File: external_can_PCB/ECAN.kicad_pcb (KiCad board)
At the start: 4 copper layers, 39.6 x 49.5 mm, 38 parts, among them J1 JST GH 4, J3 JST GH 6, J4 Micro_SD_Card, J5 JST GH 6, U1 SN65HVD232, U2 AP2127N-3.3, U5 STM32L562RETx, Y1 8 Mhz

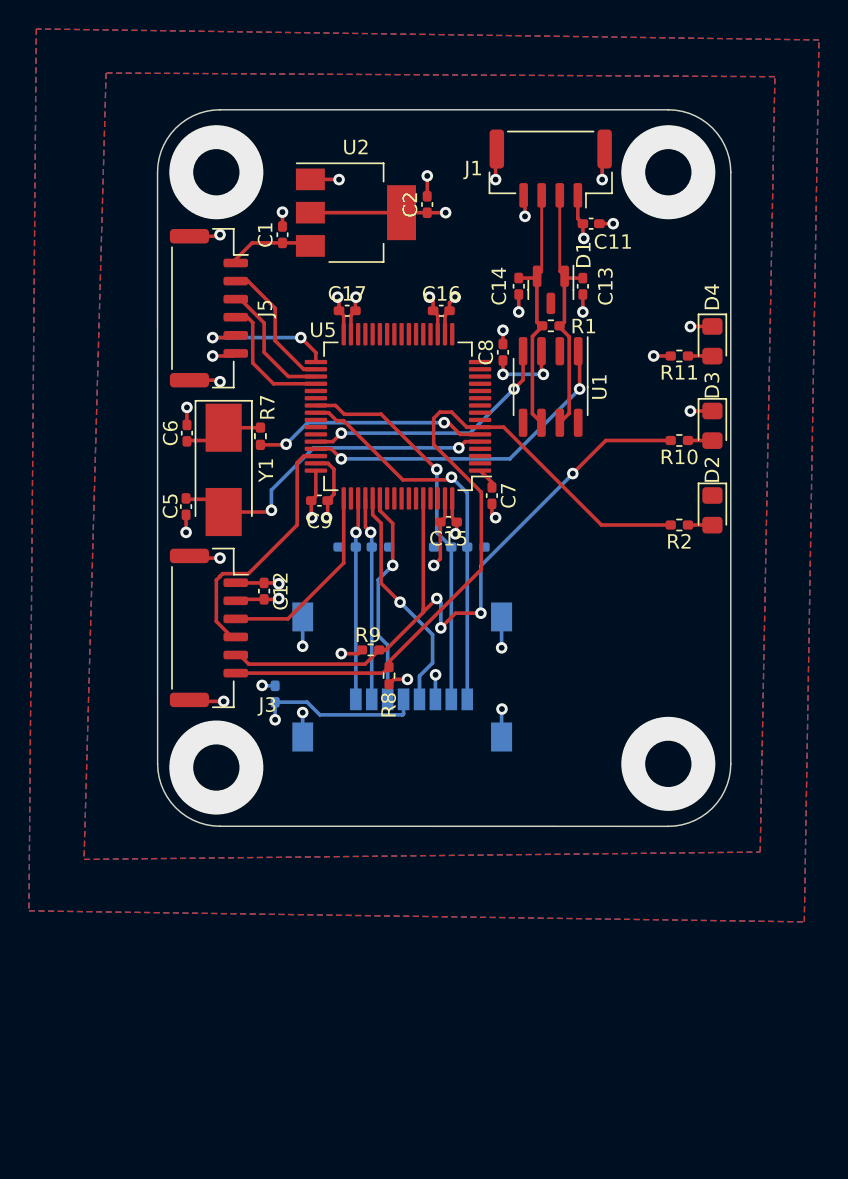
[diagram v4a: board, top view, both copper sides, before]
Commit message: Addressed issues from Review by Olof
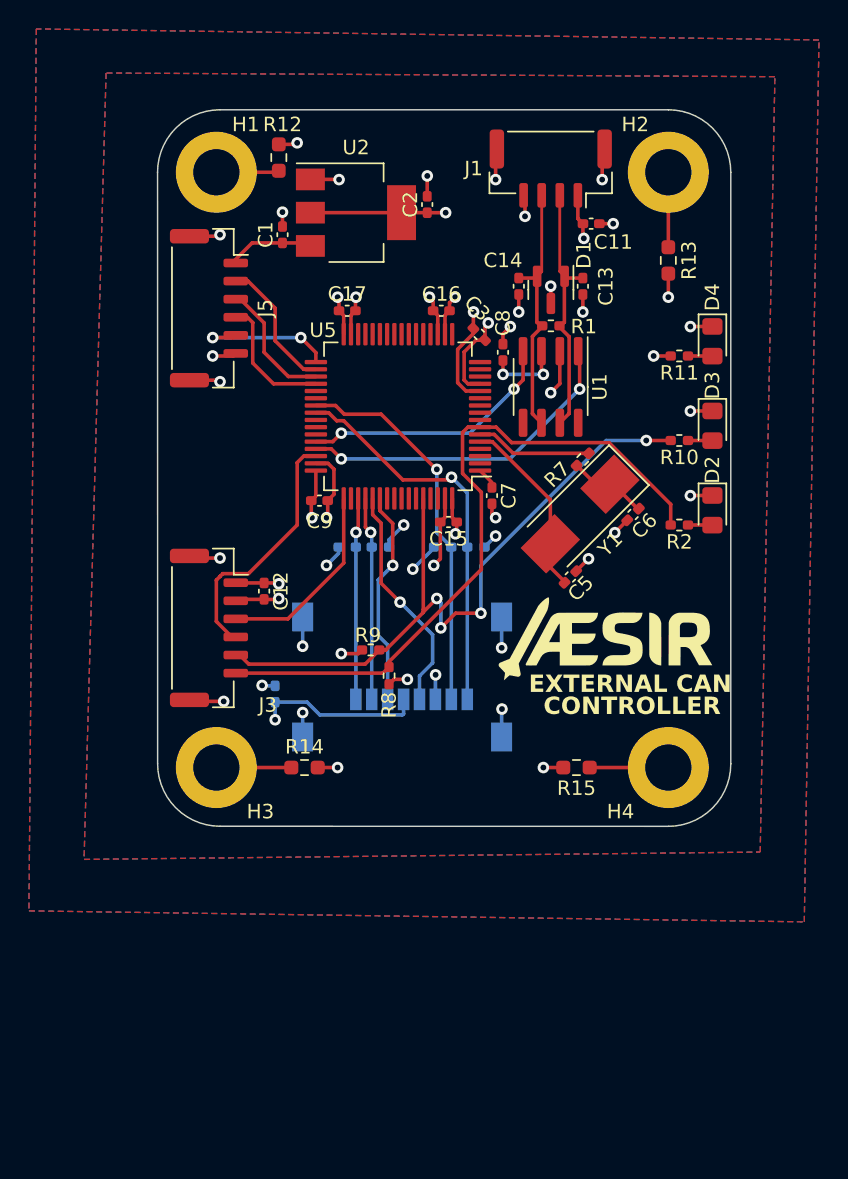
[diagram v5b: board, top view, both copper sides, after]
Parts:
- added C3: 0.1 uF, Capacitor_SMD:C_0402_1005Metric_Pad0.74x0.62mm_HandSolder, F.Cu at (142.6, 50.3)
- added G***: LOGO, LOGO, F.Cu at (151.4, 71.4)
- added H1: MountingHole_Pad, MountingHole:MountingHole_3.2mm_M3_DIN965_Pad, F.Cu at (124.5, 39.1)
- added H2: MountingHole_Pad, MountingHole:MountingHole_3.2mm_M3_DIN965_Pad, F.Cu at (155.7, 39.1)
- added H3: MountingHole_Pad, MountingHole:MountingHole_3.2mm_M3_DIN965_Pad, F.Cu at (124.5, 80.3)
- added H4: MountingHole_Pad, MountingHole:MountingHole_3.2mm_M3_DIN965_Pad, F.Cu at (155.7, 80.3)
- added R12: 1M, Resistor_SMD:R_0603_1608Metric_Pad0.98x0.95mm_HandSolder, F.Cu at (128.8, 38.1)
- added R13: 1M, Resistor_SMD:R_0603_1608Metric_Pad0.98x0.95mm_HandSolder, F.Cu at (155.7, 45.2)
- added R14: 1M, Resistor_SMD:R_0603_1608Metric_Pad0.98x0.95mm_HandSolder, F.Cu at (130.6, 80.3)
- added R15: 1M, Resistor_SMD:R_0603_1608Metric_Pad0.98x0.95mm_HandSolder, F.Cu at (149.4, 80.3)
- moved C6 31.3 mm to (153.3, 62.8), turned to -135 degrees
- moved C5 27.0 mm to (148.9, 67.1), turned to 45 degrees
- moved Y1 24.8 mm to (149.6, 62.7), turned to -135 degrees
- moved R7 22.3 mm to (149.8, 59.0), turned to -135 degrees
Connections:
- net /SPI3_MISO_3.3V renamed /SPI2_MISO_3.3V
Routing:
- net GND: track 60.9 -> 80.1 mm, vias 31 -> 39
- net +3.3V: track 47.6 -> 60.6 mm, vias 13 -> 18
- net Net-(U5-PH0): track 23.3 -> 12.3 mm, vias 2 -> 0
- net Net-(U5-PH1): track 16.2 -> 8.06 mm, vias 2 -> 0
- net Net-(H4-Pad1): track 0.00 -> 5.44 mm
- net Net-(H2-Pad1): track 0.00 -> 5.18 mm
- net Net-(H3-Pad1): track 0.00 -> 5.18 mm
- net Net-(H1-Pad1): track 0.00 -> 4.36 mm
- net /NRST: track 51.6 -> 48.2 mm
- net (no net): vias 4 -> 0
- added copper zone on B.Cu, net (none)
- added copper zone on F.Cu, net (none)
- removed copper zone on B.Cu, net /FDCAN1_RX
- removed copper zone on F.Cu, net /FDCAN1_RX
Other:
- board text added: "CONTROLLER"
- board text added: "EXTERNAL CAN"

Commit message: GPIO LED changes and UART connection to SPI lines
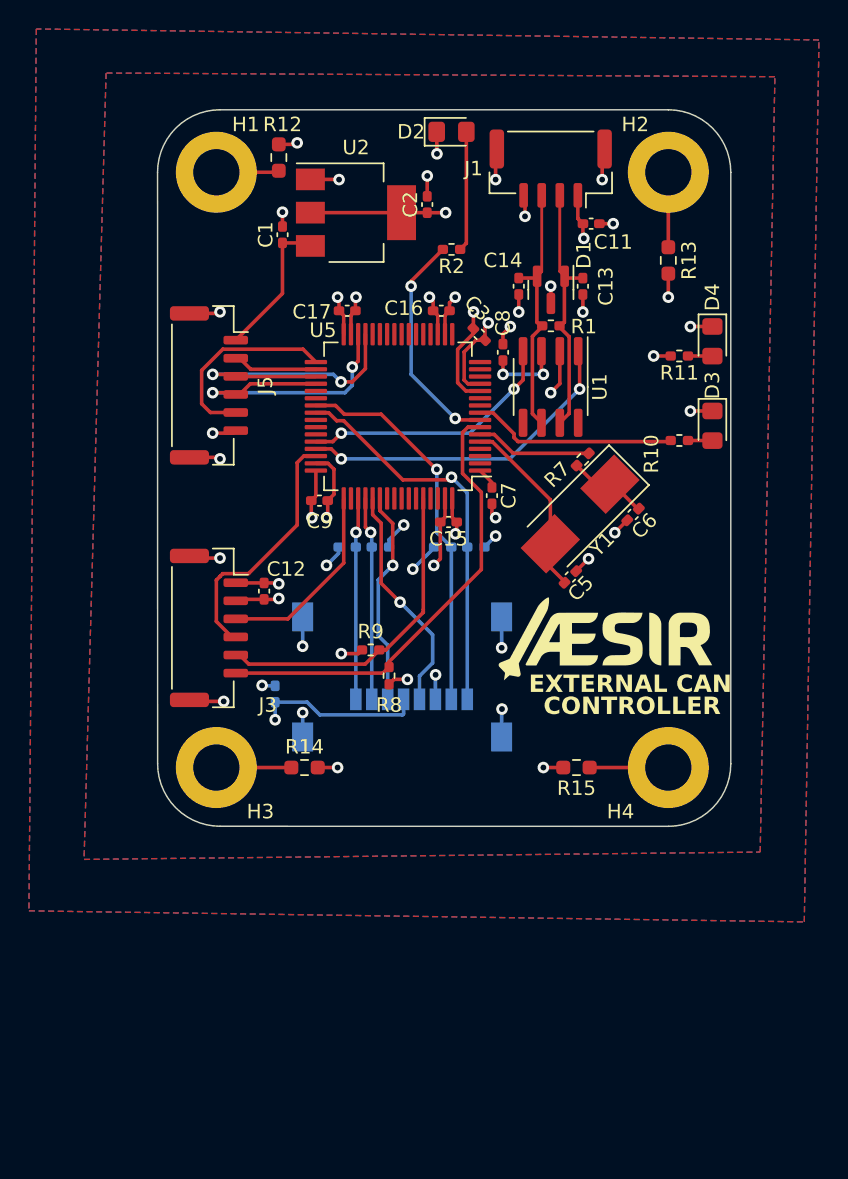
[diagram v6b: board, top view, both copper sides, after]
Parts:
- moved D2 31.8 mm to (140.7, 36.3), turned to 0 degrees
- moved R2 24.7 mm to (140.7, 44.5)
- moved J5 5.33 mm to (124.0, 53.8)
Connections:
- J5 pad 3: /SPI2_MISO_3.3V -> /SPI2_MISO_3.3V/LPUART_RX
- J5 pad 4: /SPI2_MOSI_3.3V -> /SPI2_MOSI_3.3V/LPUART_TX
- R10 pad 2: /BOOT0 -> /GPIO_ACTIVITY_1
- R2 pad 2: /NRST -> /GPIO_ACTIVITY_0
- U5 pad 29: unconnected-(U5-PB10-Pad29) -> /SPI2_MISO_3.3V/LPUART_RX
- U5 pad 30: unconnected-(U5-PB11-Pad30) -> /SPI2_MOSI_3.3V/LPUART_TX
- U5 pad 35: /SPI2_MISO_3.3V -> /SPI2_MISO_3.3V/LPUART_RX
- U5 pad 36: /SPI2_MOSI_3.3V -> /SPI2_MOSI_3.3V/LPUART_TX
- U5 pad 8: unconnected-(U5-PC0-Pad8) -> /GPIO_ACTIVITY_0
- U5 pad 9: unconnected-(U5-PC1-Pad9) -> /GPIO_ACTIVITY_1
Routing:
- net /BOOT0: track 49.2 -> 22.6 mm, vias 4 -> 0
- net /SPI2_MOSI_3.3V/LPUART_TX: track 0.00 -> 21.1 mm, vias 0 -> 2
- net /SPI2_MISO_3.3V/LPUART_RX: track 0.00 -> 20.7 mm, vias 0 -> 2
- net /NRST: track 48.2 -> 31.4 mm
- net /GPIO_ACTIVITY_0: track 0.00 -> 15.6 mm, vias 0 -> 2
- net /GPIO_ACTIVITY_1: track 0.00 -> 14.2 mm
- net /SPI2_MOSI_3.3V: track 9.08 -> 0.00 mm
- net /SPI2_MISO_3.3V: track 8.94 -> 0.00 mm
- net Net-(D2-A): track 1.69 -> 8.31 mm
- net Net-(J5-Pin_1): track 6.08 -> 10.1 mm
- net /SPI2_NSS_3.3V: track 9.88 -> 13.8 mm, vias 2 -> 0
- net /SPI2_SCK_3.3V: track 9.38 -> 5.85 mm

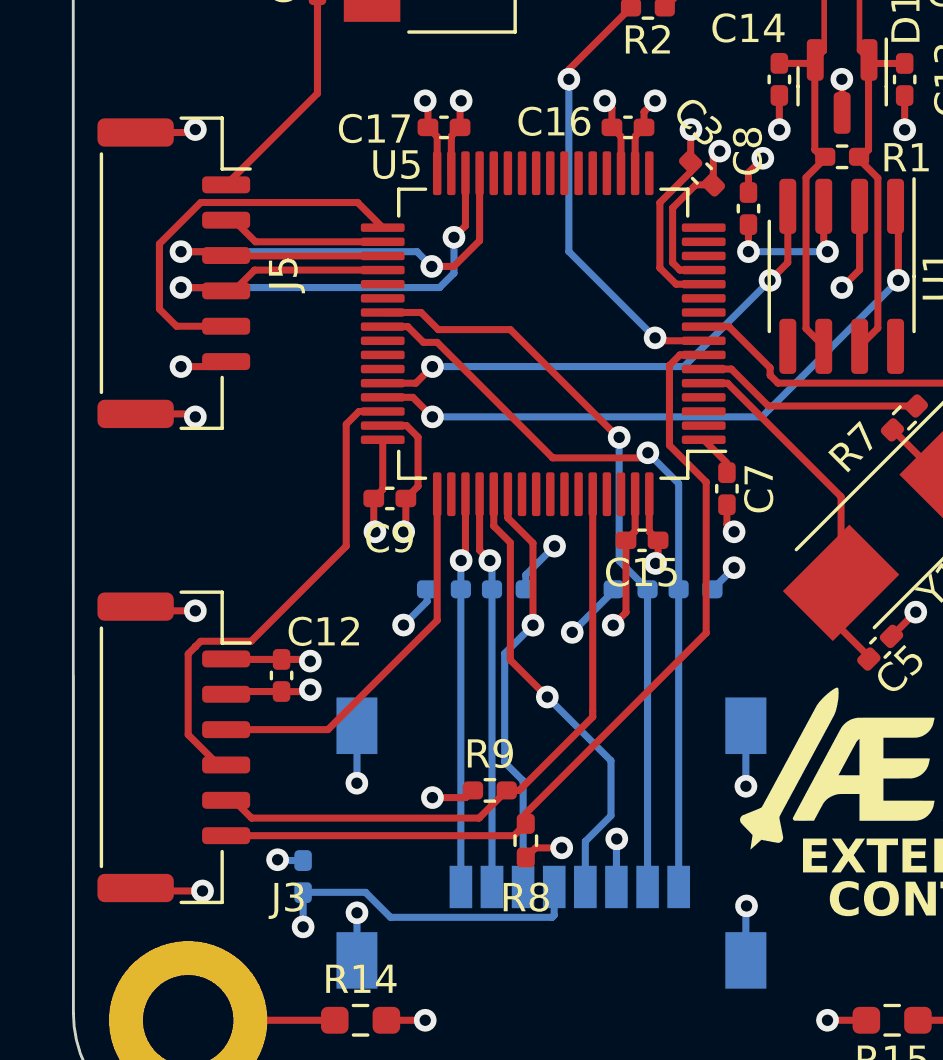
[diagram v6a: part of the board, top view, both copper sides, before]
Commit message: final length matching
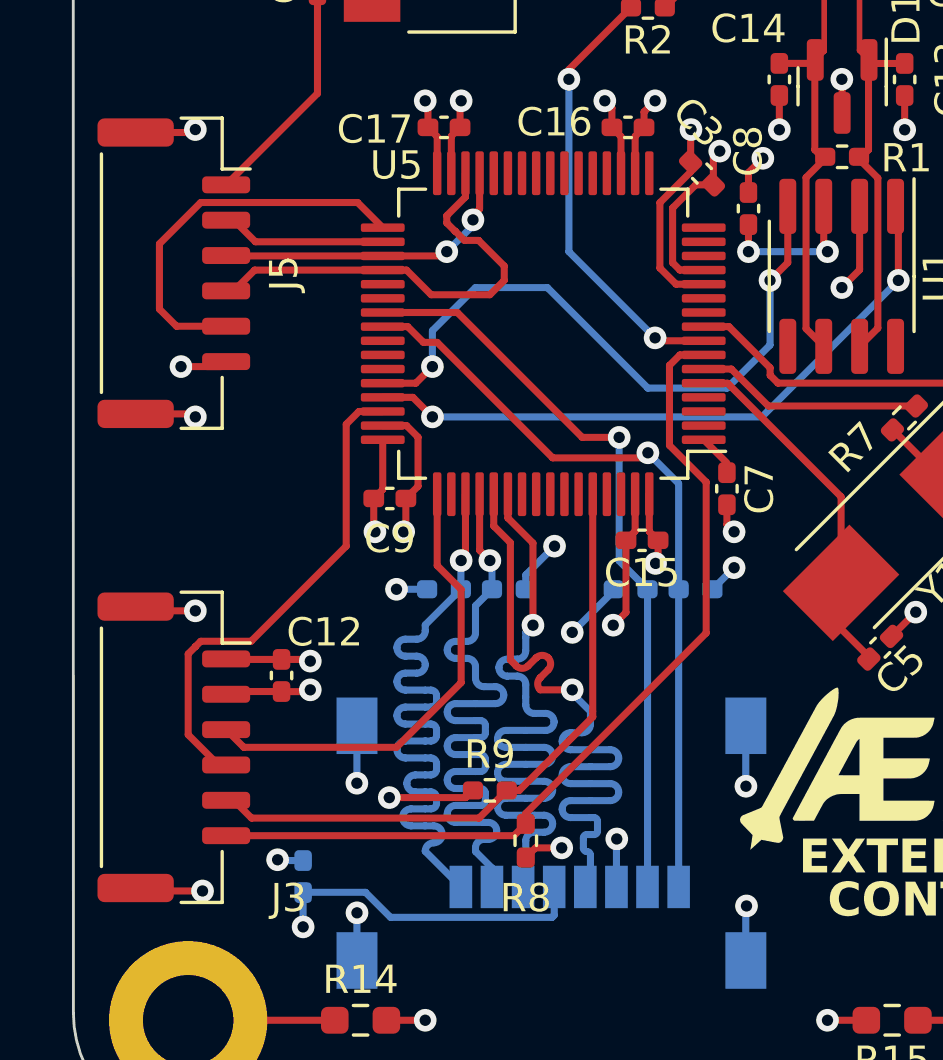
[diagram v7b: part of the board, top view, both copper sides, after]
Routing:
- net Net-(J4-DAT2): track 14.0 -> 27.0 mm
- net Net-(J4-DAT3/CD): track 14.1 -> 27.1 mm
- net Net-(J4-CMD): track 14.9 -> 27.2 mm
- net Net-(J4-CLK): track 16.0 -> 26.6 mm
- net /SPI2_MISO_3.3V/LPUART_RX: track 20.7 -> 11.1 mm
- net /SPI2_MOSI_3.3V/LPUART_TX: track 21.1 -> 15.9 mm, vias 2 -> 0
- net /FDCAN1_RX: track 18.1 -> 23.1 mm
- net /JTCK/SWCLK: track 13.5 -> 16.5 mm
- net GND: track 80.1 -> 81.6 mm
- net +3.3V: track 60.6 -> 60.1 mm

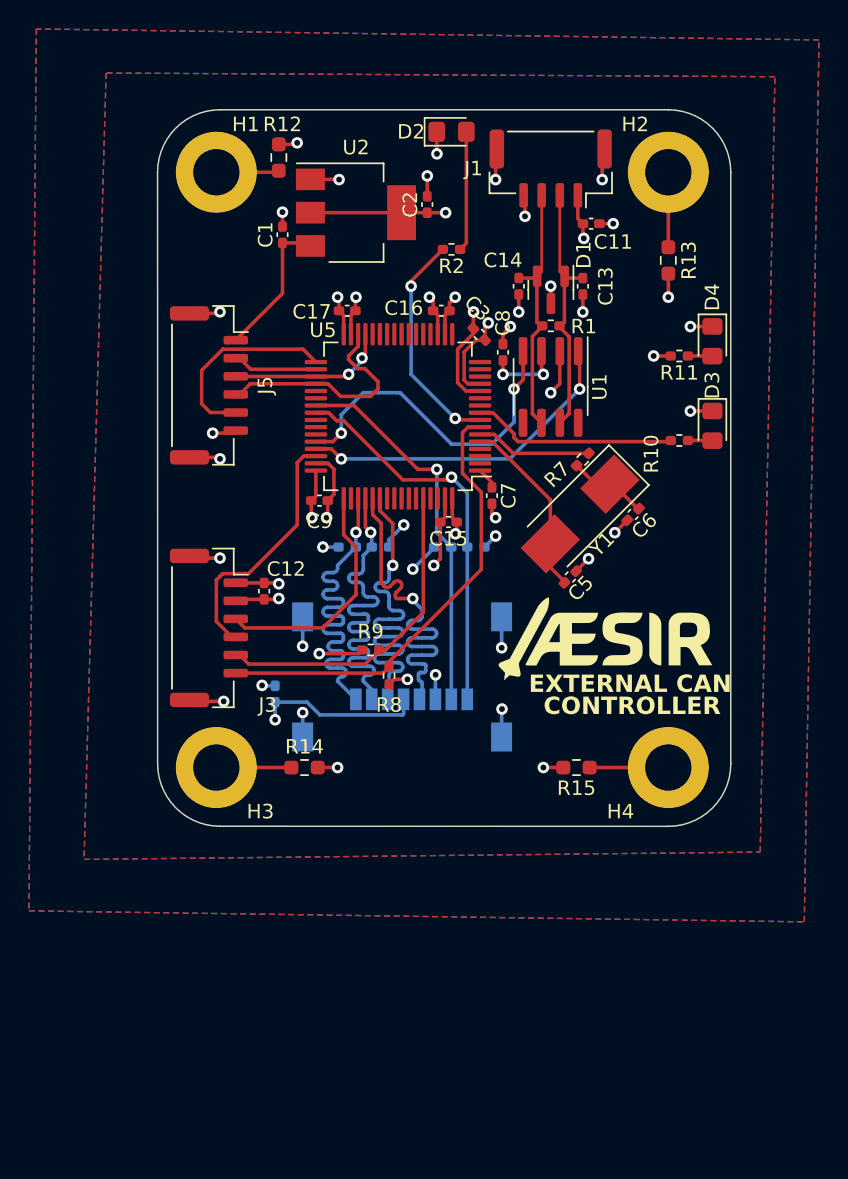
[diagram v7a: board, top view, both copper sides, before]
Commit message: Changed CAN connecter reference to 5V, which allows the board to be powered through the CAN connector
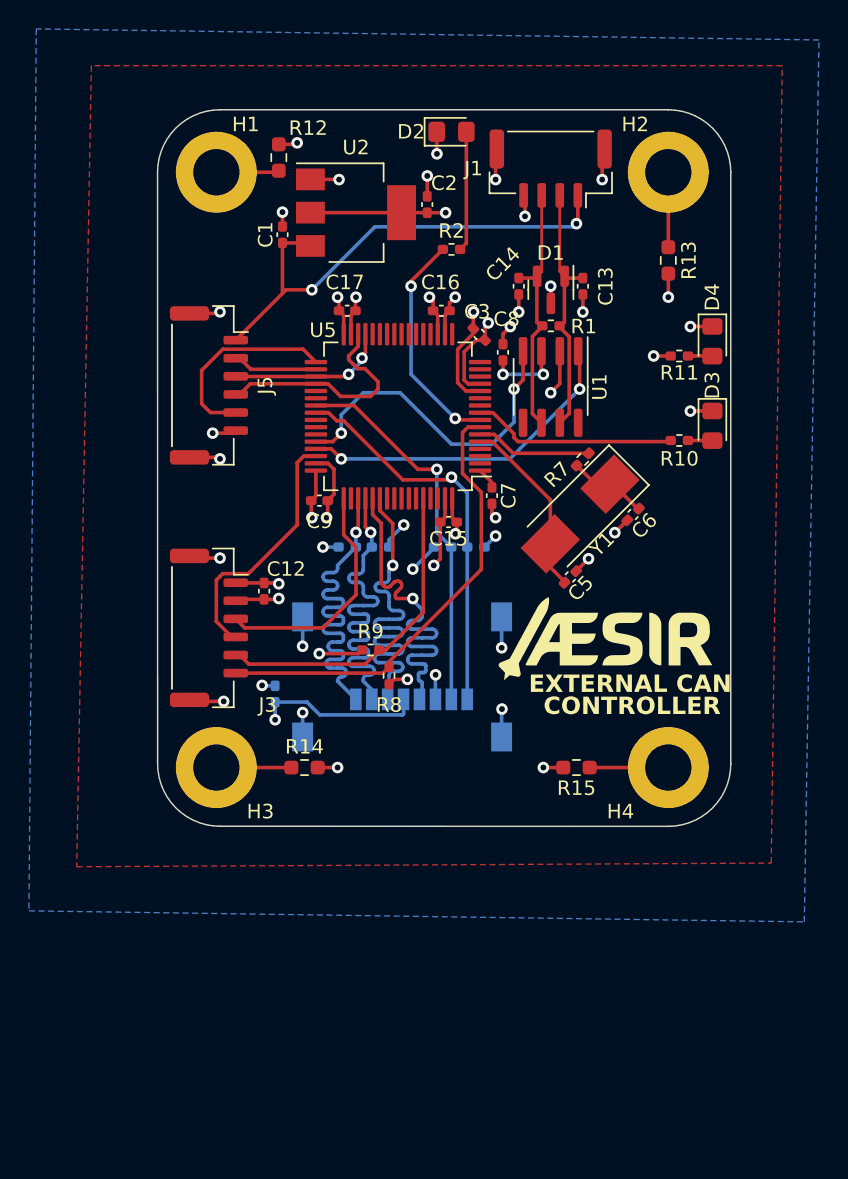
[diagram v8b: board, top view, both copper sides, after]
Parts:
- removed C11: 0.1 uF, Capacitor_SMD:C_0402_1005Metric_Pad0.74x0.62mm_HandSolder
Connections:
- J1 pad 1: +3.3V -> Net-(#FLG01-pwr)
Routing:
- net Net-(#FLG01-pwr): track 10.1 -> 34.4 mm, vias 0 -> 2
- net +3.3V: track 60.1 -> 56.9 mm, vias 18 -> 17
- net GND: track 81.6 -> 80.6 mm, vias 39 -> 38
- added copper zone on B.Cu, net GND
- added copper zone on F.Cu, net GND
- removed copper zone on B.Cu, net (none)
- removed copper zone on F.Cu, net (none)
- removed copper zone on B.Cu, net /BOOT0
- removed copper zone on F.Cu, net /BOOT0
